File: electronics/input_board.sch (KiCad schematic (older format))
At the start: 16 parts, among them P3 CONN_01X02, Q1 IRLZ44N, Q2 IRF9Z34, Q3 IRLZ44N, Q4 IRLZ44N

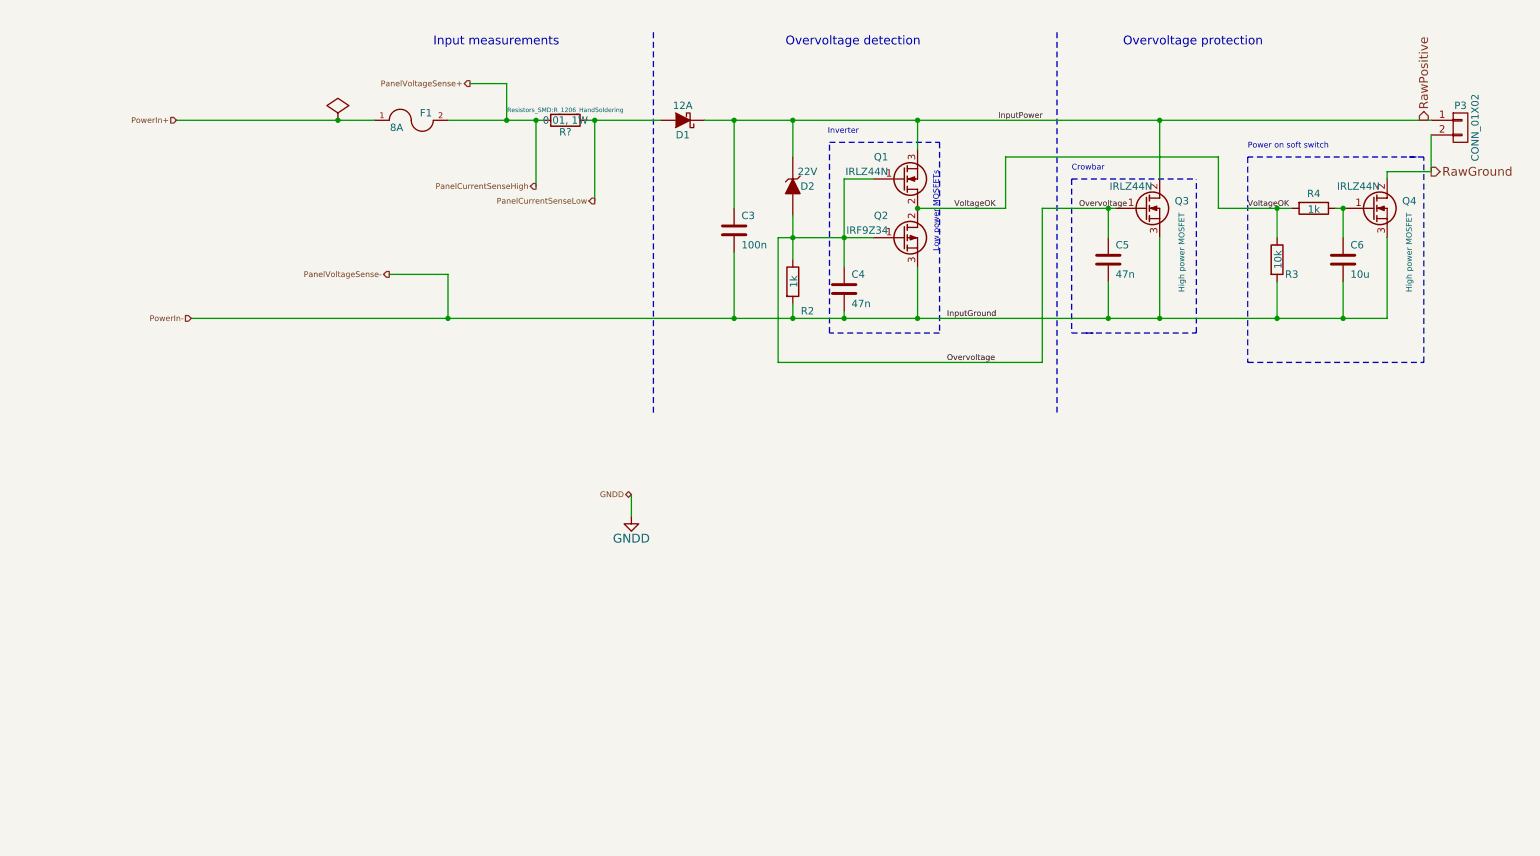
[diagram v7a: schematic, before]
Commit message: redoing power supply as an 5A one
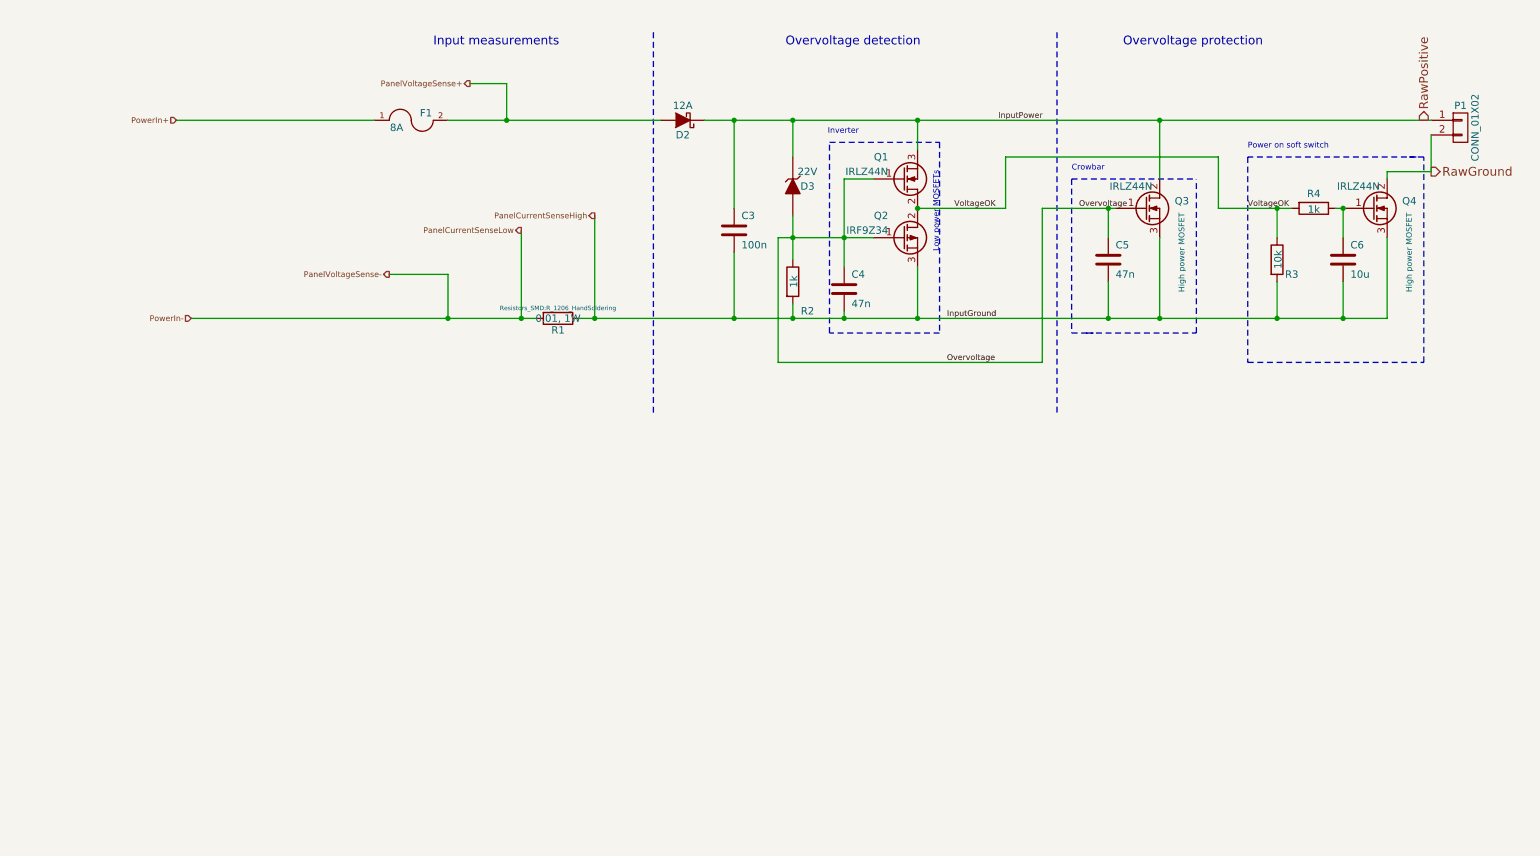
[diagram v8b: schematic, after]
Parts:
- D3: renamed from D2; footprint Diodes_SMD:Diode-SMC_Handsoldering -> Diodes_SMD:Diode-SMB_Standard
- gave numbers to parts that had none: 1
- renumbered D1 to D2, P3 to P1
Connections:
- net PanelVoltageSense- is gone; now on net PanelCurrentSenseHigh: C3.2, C4.2, C5.2, C6.2, Q2.3 (S), Q3.3 (S), Q4.3 (S), R2.2, R3.2
- net PanelCurrentSenseHigh: now also R1.1; no longer F1.2, R1.2
- net PanelCurrentSenseLow: now also R1.2; no longer D2.2 (A), R1.1
- new net PanelVoltageSense+: D2.2 (A), F1.2
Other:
- moved on the sheet: R1
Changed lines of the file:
@@
 $Descr A4 11693 8268
 encoding utf-8
-Sheet 2 3
+Sheet 3 3
 Title "Sunpowered Input Board"
 Date ""
@@
 $EndDescr
 $Comp
-L ZENER D2
+L ZENER D3
 U 1 1 55E0D9D5
 P 5750 1750
-F 0 "D2" V 5750 1850 50  0000 C CNN
+F 0 "D3" V 5750 1850 50  0000 C CNN
 F 1 "22V" V 5650 1850 50  0000 C CNN
-F 2 "Diodes_SMD:Diode-SMC_Handsoldering" H 5750 1750 60  0001 C CNN
-F 3 "http://www.comchiptech.com/cms/UserFiles/ACZRC5333B-G%20Thru.%20ACZRC5388B-G%20RevA.pdf" H 5750 1750 60  0001 C CNN
-F 4 "~" V 5850 1400 39  0000 C CNN "Note"
+F 2 "Diodes_SMD:Diode-SMB_Standard" H 5750 1750 60  0001 C CNN
+F 3 "http://www.tme.eu/pl/Document/c2d23b0bf5a10da03f2379b0c2e473b6/1SMB5913BT3-D.PDF" H 5750 1750 60  0001 C CNN
 	1    5750 1750
 	0    1    1    0
@@
 Power on soft switch
 $Comp
-L CONN_01X02 P3
+L CONN_01X02 P1
 U 1 1 55E0DA62
 P 10300 1350
-F 0 "P3" H 10300 1500 50  0000 C CNN
+F 0 "P1" H 10300 1500 50  0000 C CNN
 F 1 "CONN_01X02" V 10400 1350 50  0000 C CNN
 F 2 "Terminal_Blocks:TerminalBlock_WAGO-236_2Stift_RM5mm_2pol" H 10300 1350 60  0001 C CNN
@@
 	9800 1650 10100 1650
 Wire Wire Line
-	3400 1300 3800 1300
-Wire Wire Line
-	3800 1300 4000 1300
-Wire Wire Line
-	4000 1300 4050 1300
-Wire Wire Line
-	1550 1300 2650 1300
-Wire Wire Line
-	2650 1300 2900 1300
+	3400 1300 4850 1300
+Wire Wire Line
+	1550 1300 2900 1300
 Wire Wire Line
 	3800 1050 3800 1300
@@
 	5750 1300 5750 1550
 Wire Wire Line
-	5750 1950 5750 2100
-Wire Wire Line
-	5750 2100 5750 2250
+	5750 1950 5750 2250
 Connection ~ 5750 2100
 Connection ~ 9050 2650
@@
 	9800 2650 9800 2100
 Wire Wire Line
-	5150 1300 5350 1300
-Wire Wire Line
-	5350 1300 5750 1300
-Wire Wire Line
-	5750 1300 6600 1300
-Wire Wire Line
-	6600 1300 8250 1300
-Wire Wire Line
-	8250 1300 10100 1300
+	5150 1300 10100 1300
 Wire Wire Line
 	3400 2350 3400 2650
-Connection ~ 3400 2650
 Wire Wire Line
 	3400 2350 3000 2350
 Wire Wire Line
 	10100 1650 10100 1400
-$Comp
-L PWR_FLAG #FLG09
-U 1 1 55E0DAAC
-P 2650 1300
-F 0 "#FLG09" H 2650 1395 30  0001 C CNN
-F 1 "PWR_FLAG" H 2650 1480 30  0001 C CNN
-F 2 "" H 2650 1300 60  0000 C CNN
-F 3 "" H 2650 1300 60  0000 C CNN
-	1    2650 1300
-	1    0    0    -1
-$EndComp
 Wire Wire Line
 	9450 1900 9500 1900
@@
 	5750 2650 5750 2550
 $Comp
-L D_Schottky D1
+L D_Schottky D2
 U 1 1 55EBE3EF
 P 5000 1300
-F 0 "D1" H 5000 1400 50  0000 C CNN
+F 0 "D2" H 5000 1400 50  0000 C CNN
 F 1 "12A" H 5000 1200 50  0000 C CNN
 F 2 "Diodes_SMD:D-Pak_TO252AA" H 5000 1300 60  0001 C CNN
@@
 RawGround
 Wire Wire Line
-	5650 2100 5750 2100
-Wire Wire Line
-	5750 2100 6100 2100
-Wire Wire Line
-	6100 2100 6300 2100
+	5650 2100 6300 2100
 $Comp
 L Q_NMOS_GDS Q4
@@
 $EndComp
 Wire Wire Line
-	6100 1700 6100 2100
-Wire Wire Line
-	6100 2100 6100 2300
+	6100 1700 6100 2300
 Wire Wire Line
 	6100 1700 6300 1700
@@
 Overvoltage
 Wire Wire Line
-	4350 1300 4400 1300
-Wire Wire Line
-	4400 1300 4850 1300
-Wire Wire Line
-	1650 2650 3400 2650
-Wire Wire Line
-	3400 2650 5350 2650
-Wire Wire Line
-	5350 2650 5750 2650
-Wire Wire Line
-	5750 2650 6100 2650
-Wire Wire Line
-	6100 2650 6600 2650
-Wire Wire Line
-	6600 2650 7900 2650
-Wire Wire Line
-	7900 2650 8250 2650
-Wire Wire Line
-	8250 2650 9050 2650
-Wire Wire Line
-	9050 2650 9500 2650
-Wire Wire Line
-	9500 2650 9800 2650
-Wire Wire Line
-	8650 1900 9050 1900
-Wire Wire Line
-	9050 1900 9150 1900
+	4300 2650 9800 2650
+Wire Wire Line
+	8650 1900 9150 1900
 Text Label 8850 1900 0    39   ~ 0
 VoltageOK
@@
 InputPower
 Wire Wire Line
-	7450 1900 7900 1900
-Wire Wire Line
-	7900 1900 7950 1900
+	7450 1900 7950 1900
 Text Label 7700 1900 0    39   ~ 0
 Overvoltage
@@
 Text Notes 7650 1650 0    39   ~ 0
 Crowbar
-Text HLabel 4000 1750 0    39   Output ~ 0
+Text HLabel 4400 1950 0    39   Output ~ 0
 PanelCurrentSenseHigh
-Text HLabel 4650 3850 0    39   BiDi ~ 0
-GNDD
-$Comp
-L GNDD #PWR011
-U 1 1 566DB00E
-P 4650 4000
-F 0 "#PWR011" H 4650 3750 60  0001 C CNN
-F 1 "GNDD" H 4650 3850 60  0000 C CNN
-F 2 "" H 4650 4000 60  0000 C CNN
-F 3 "" H 4650 4000 60  0000 C CNN
-	1    4650 4000
-	1    0    0    -1
-$EndComp
-Wire Wire Line
-	4650 3850 4650 4000
 Text HLabel 3000 2350 0    39   Output ~ 0
 PanelVoltageSense-
@@
 Text HLabel 1650 2650 0    39   Input ~ 0
 PowerIn-
-Connection ~ 2650 1300
 Text HLabel 1550 1300 0    39   Input ~ 0
 PowerIn+
 $Comp
-L R R?
+L R R1
 U 1 1 56756EEE
-P 4200 1300
-F 0 "R?" V 4280 1300 50  0000 C CNN
-F 1 "0.01, 1W" V 4200 1300 50  0000 C CNN
-F 2 "Resistors_SMD:R_1206_HandSoldering" V 4130 1300 30  0000 C CNN
-F 3 "" H 4200 1300 30  0000 C CNN
-	1    4200 1300
+P 4150 2650
+F 0 "R1" V 4230 2650 50  0000 C CNN
+F 1 "0.01, 1W" V 4150 2650 50  0000 C CNN
+F 2 "Resistors_SMD:R_1206_HandSoldering" V 4080 2650 30  0000 C CNN
+F 3 "" H 4150 2650 30  0000 C CNN
+	1    4150 2650
 	0    1    1    0
 $EndComp
-Wire Wire Line
-	4000 1300 4000 1750
-Connection ~ 4000 1300
-Wire Wire Line
-	4400 1300 4400 1850
-Connection ~ 4400 1300
-Text HLabel 4400 1850 0    39   Output ~ 0
+Text HLabel 3900 2050 0    39   Output ~ 0
 PanelCurrentSenseLow
+Wire Wire Line
+	4400 1950 4400 2650
+Connection ~ 4400 2650
+Wire Wire Line
+	3900 2650 3900 2050
+Connection ~ 3900 2650
+Wire Wire Line
+	1650 2650 4000 2650
+Connection ~ 3400 2650
 $EndSCHEMATC
